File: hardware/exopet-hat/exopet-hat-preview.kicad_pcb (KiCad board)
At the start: 2 copper layers, 65 x 56 mm, 20 parts, among them J1 BarrelJack_CUI_PJ-102AH_Horiz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, J10 TerminalBlock_Phoenix_MKDS-1,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, J11 TerminalBlock_Phoenix_MKDS-1,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, J12 PinSocket_1x03_P2.54mm_Vertic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, J2 TerminalBlock_Phoenix_MKDS-1,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, J3 PinSocket_2x20_P2.54mm_Vertic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, J4 Jack_3.5mm_CUI_SJ-3523-SMT_Ho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, J6 BNC_Amphenol_B6252HB-NPP3G-50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, J7 PinSocket_1x03_P2.54mm_Vertic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, J8 TerminalBlock_Phoenix_MKDS-1,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, J9 TerminalBlock_Phoenix_MKDS-1,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, K1 Relay_SPDT_Omron-G5LE-1, K2 Relay_SPDT_Omron-G5LE-1, K3 Relay_SPDT_Omron-G5LE-1, K4 Relay_SPDT_Omron-G5LE-1

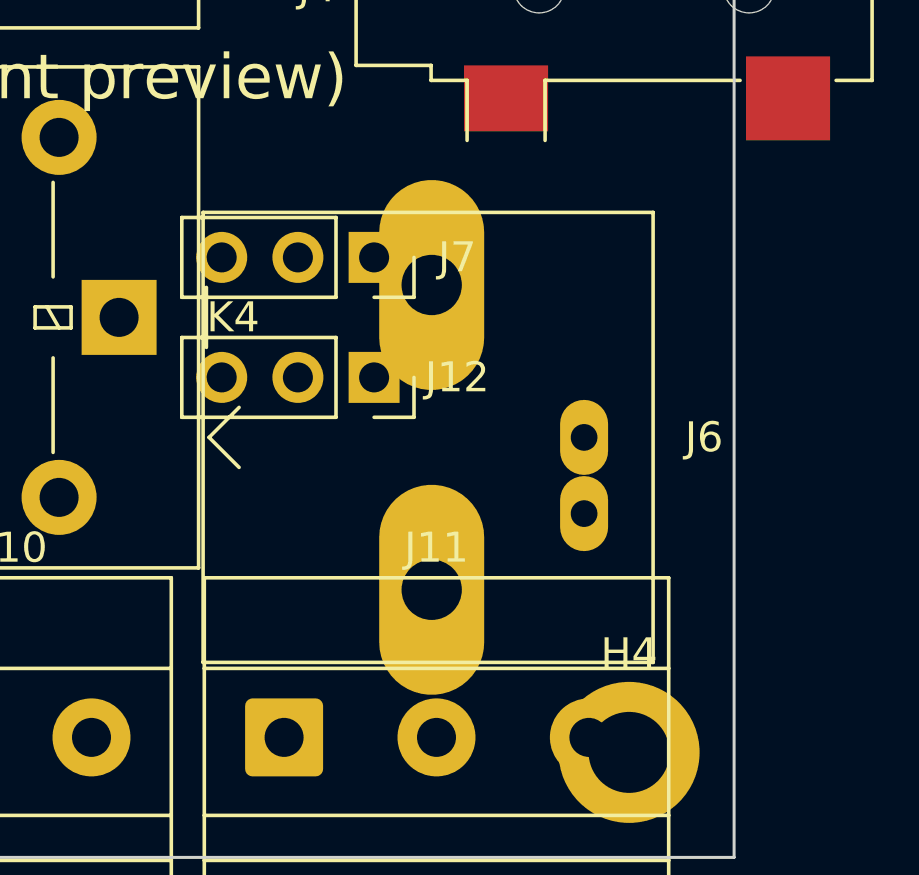
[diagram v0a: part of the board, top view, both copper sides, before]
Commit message: Drop pH from HAT rev 1; defer to isolated rev 2 design
Per Atlas EZO-pH datasheet isolation requirements near pumps/valves.
BNC and EZO sockets removed from schematic and preview; GPIO2/3 left
unconnected and reserved. ERC still clean; netlist re-verified with
pH nets and parts confirmed absent, EEPROM path intact.

Co-Authored-By: Claude Fable 5 <noreply@anthropic.com>
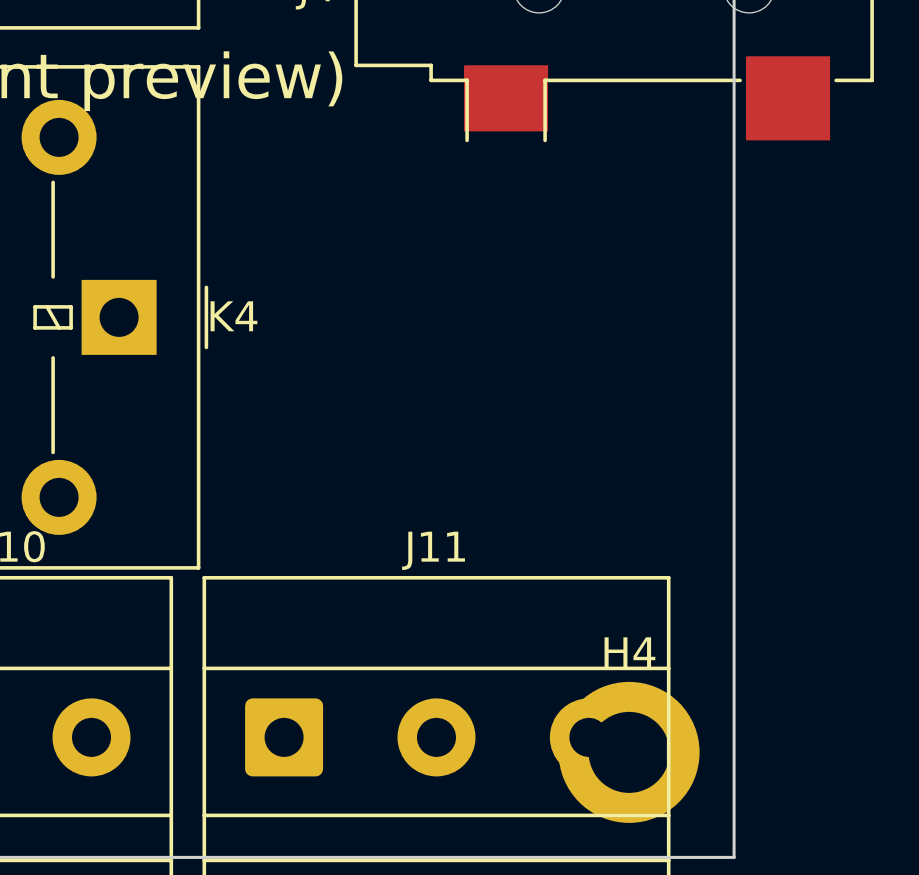
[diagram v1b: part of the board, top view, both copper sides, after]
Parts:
- removed J12, J7: PinSocket_1x03_P2.54mm_Vertical, Connector_PinSocket_2.54mm:PinSocket_1x03_P2.54mm_Vertical
- removed J6: BNC_Amphenol_B6252HB-NPP3G-50_Horizontal, Connector_Coaxial:BNC_Amphenol_B6252HB-NPP3G-50_Horizontal
